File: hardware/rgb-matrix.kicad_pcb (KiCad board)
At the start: 4 copper layers, 58 x 58 mm, 84 parts, among them CON1 VEXT, P1 MATRIX_BOT, P10 PSOUTH, P11 PEAST, P12 WEST, P13 NORTH, P14 SOUTH, P15 EAST, P2 MATRIX_TOP, P3 SWD, P4 SPI3, P5 UART5, P6 VEXT, P7 USB_B, P8 PWEST, P9 PNORTH, SW1 RESET, SW2 BOOT, U1 74AC244, U2 74AC244, U3 74AC244, U4 ULN2803A, U5 STM32F405R, U6 LD3985M33R, U7 USBUFxxW6, X1 8MHz

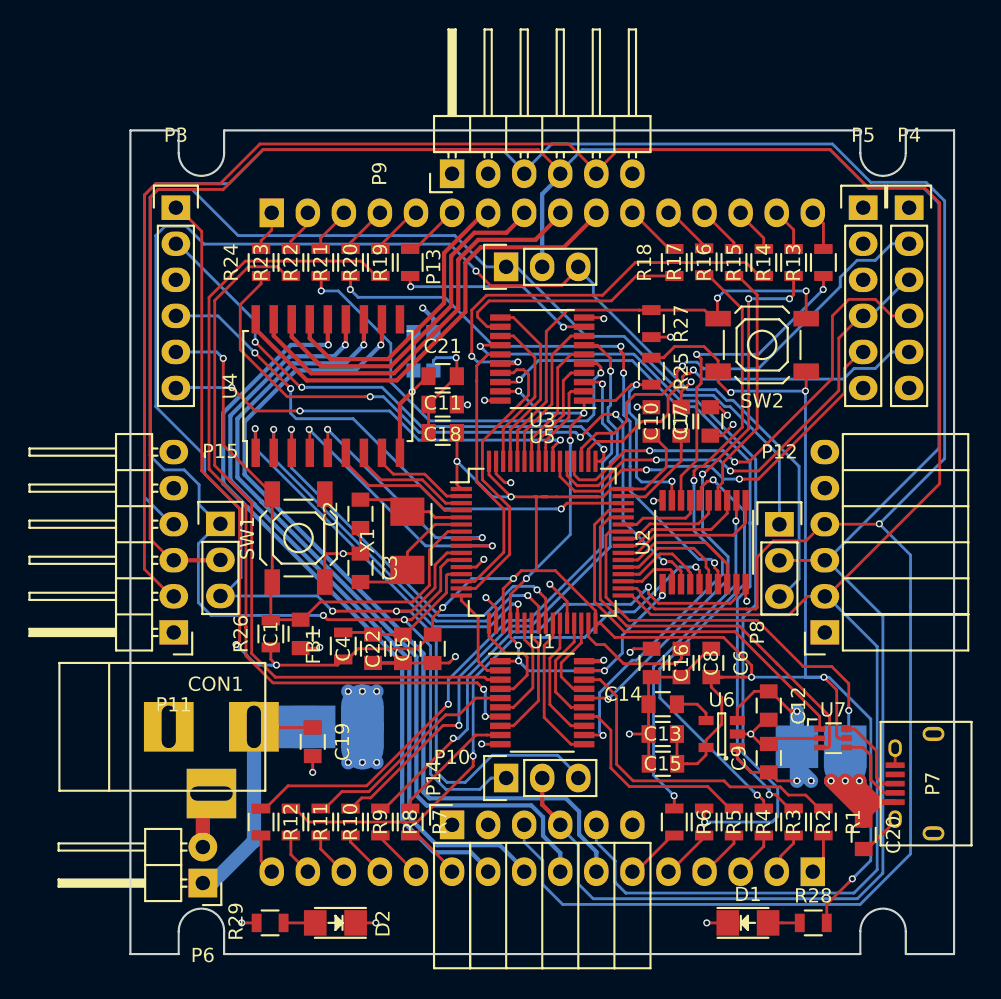
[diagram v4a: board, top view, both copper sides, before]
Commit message: Fix silkscreen
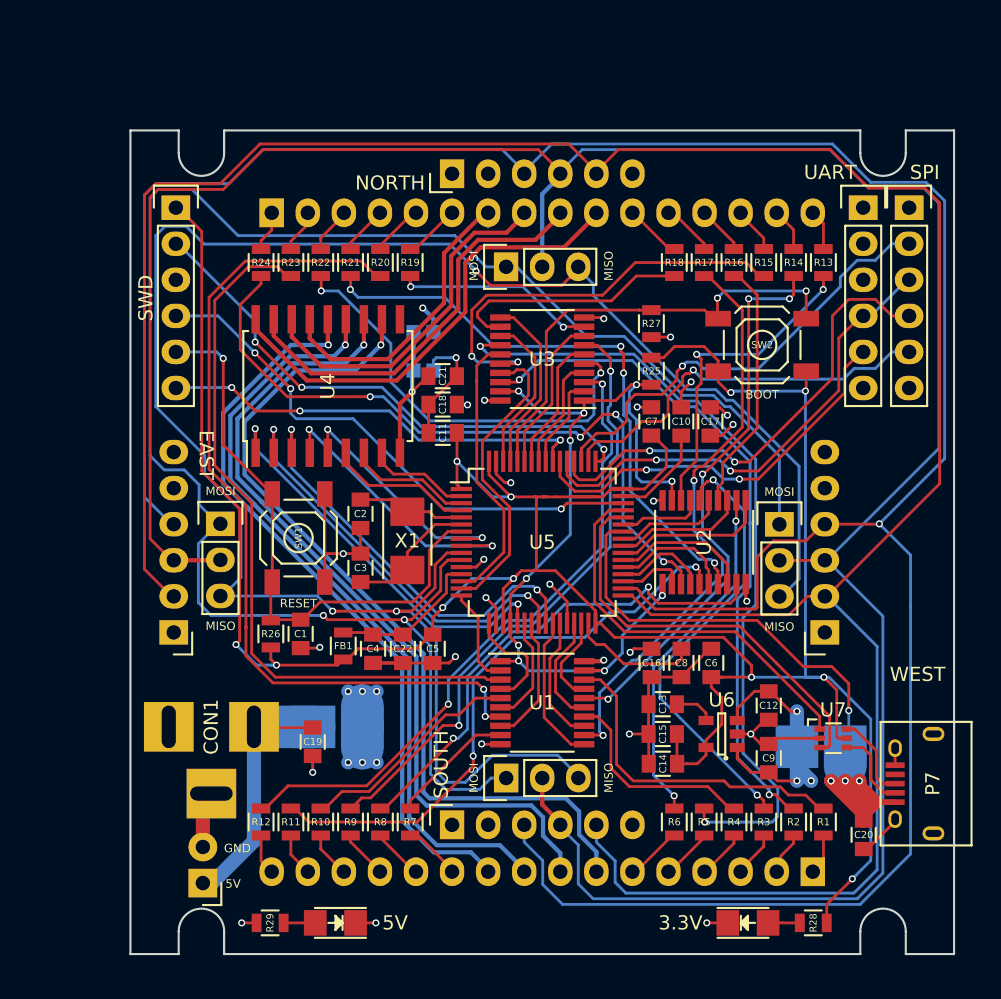
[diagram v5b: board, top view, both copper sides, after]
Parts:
- C1, C10, C11, C12, C13, C14, C15, C16, C17, C18, C19, C2, C20, C21, C22, C3, C4, C5, C6, C7, C8, C9: footprint Capacitors_SMD:C_0805 -> rgb-matrix:C_0805
- CON1: footprint Connect:BARREL_JACK -> rgb-matrix:BARREL_JACK
- FB1, R1, R10, R11, R12, R13, R14, R15, R16, R17, R18, R19, R2, R20, R21, R22, R23, R24, R25, R26, R27, R28, R29, R3, R4, R5, R6, R7, R8, R9: footprint Resistors_SMD:R_0805 -> rgb-matrix:R_0805
- P10, P8: footprint Socket_Strips:Socket_Strip_Angled_1x06 -> rgb-matrix:Socket_Strip_Angled_1x06
- P11, P9: footprint Pin_Headers:Pin_Header_Angled_1x06 -> rgb-matrix:Pin_Header_Angled_1x06
- P6: footprint Pin_Headers:Pin_Header_Angled_1x02 -> rgb-matrix:Pin_Header_Angled_1x02
- moved R17 0.05 mm to (173.6, 81.5)
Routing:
- net /power/VEXT: track 23.5 -> 21.4 mm
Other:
- board text added: "3.3V"
- board text added: "5V"
- board text added: "BOOT"
- board text added: "BOTTOM"
- board text added: "EAST"
- board text added: "GND"
- board text added: "MISO"
- board text added: "MOSI"
- board text added: "NORTH"
- board text added: "RESET"
- board text added: "SOUTH"
- board text added: "SPI"
- board text added: "SWD"
- board text added: "TOP"
- board text added: "UART"
- board text added: "WEST"

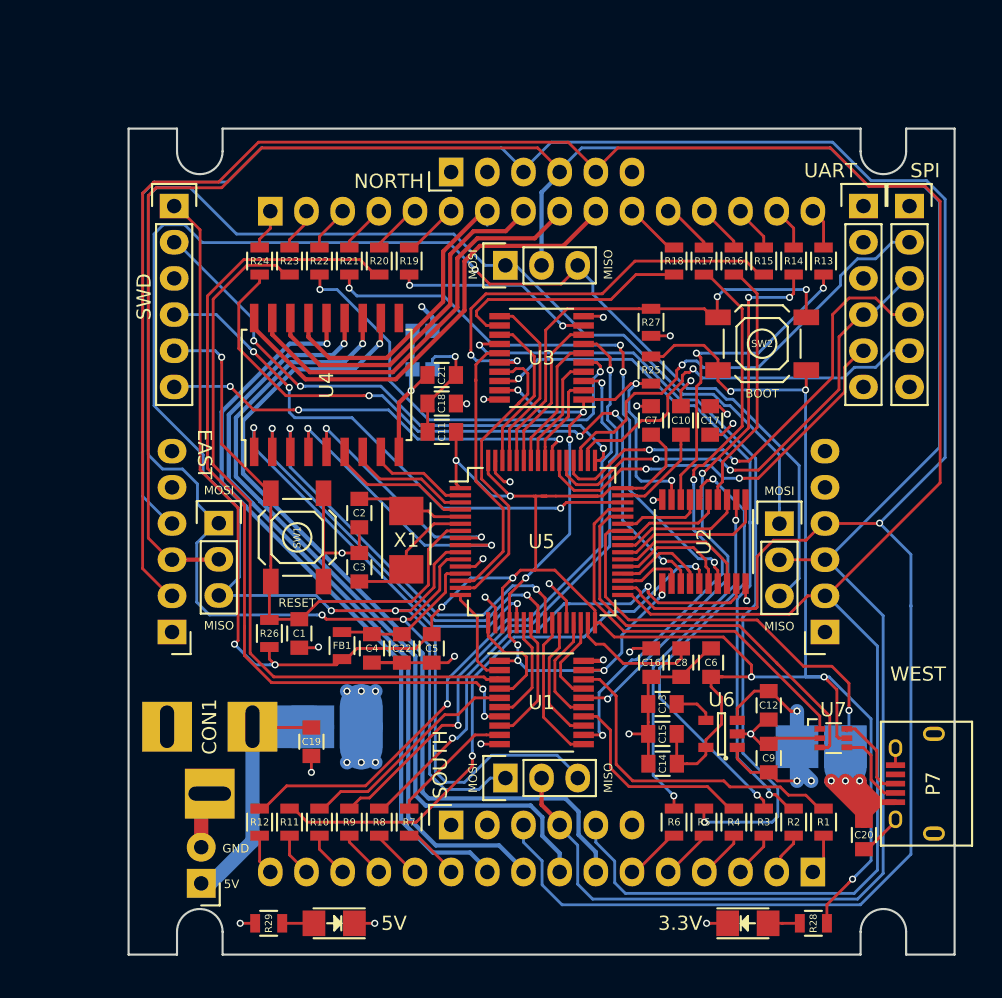
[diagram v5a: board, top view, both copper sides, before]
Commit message: Add 2nd GND pin for more curent + minor changes
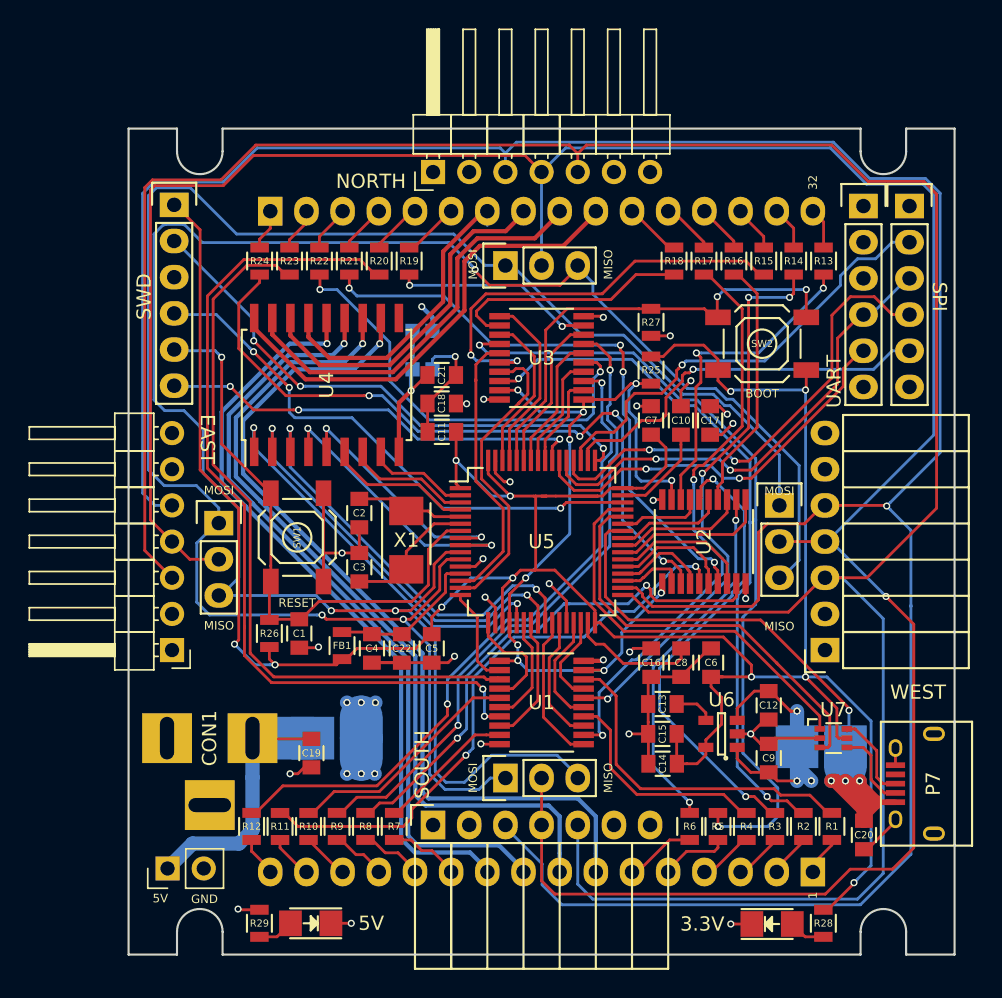
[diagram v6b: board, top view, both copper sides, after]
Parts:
- C16, C17, C18, C21: value 100n -> 100nF
- C2, C3: value 18pF -> 26pF
- P10, P8: footprint rgb-matrix:Socket_Strip_Angled_1x06 -> Socket_Strips:Socket_Strip_Angled_1x07
- P11, P9: footprint rgb-matrix:Pin_Header_Angled_1x06 -> Pin_Headers:Pin_Header_Angled_1x07_Pitch2.54mm
- P6: footprint rgb-matrix:Pin_Header_Angled_1x02 -> Pin_Headers:Pin_Header_Straight_1x02_Pitch2.54mm
- U7: value USBUFxxW6 -> USBUF01W6
- moved P6 2.59 mm to (135.9, 124.2), turned to 90 degrees
- moved D1 1.70 mm to (178.3, 128.1)
- moved D2 1.65 mm to (145.9, 128.0)
- moved P12 1.28 mm to (178.9, 98.7)
- moved P11 1.27 mm to (136.2, 108.8)
- moved P8 1.27 mm to (182.1, 108.8)
- moved P10 1.27 mm to (154.5, 121.1)
- moved P9 1.27 mm to (154.5, 75.2)
- moved R6 1.14 mm to (172.6, 121.2)
- moved R7 1.09 mm to (151.8, 121.2)
- moved R5 1.03 mm to (174.6, 121.2)
- moved R8 1.01 mm to (149.8, 121.2)
- moved R4 0.94 mm to (176.6, 121.2)
- moved R9 0.91 mm to (147.8, 121.2)
- moved R3 0.84 mm to (178.6, 121.2)
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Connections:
- P11 pad 2: SPI2_NSS -> GND
- P11 pad 3: /daisy/DATA -> SPI2_NSS
- P11 pad 4: SPI2_SCK -> /daisy/DATA
- P11 pad 5: +5V -> SPI2_SCK
- P8 pad 2: SPI2_NSS -> GND
- P8 pad 3: /daisy/DATA -> SPI2_NSS
- P8 pad 4: SPI2_SCK -> /daisy/DATA
- P8 pad 5: +5V -> SPI2_SCK
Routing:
- net SPI2_NSS: track 181.2 -> 185.8 mm
- net GND: track 82.3 -> 77.7 mm
- net +5V: track 44.5 -> 46.1 mm
- net +3V3: track 198.2 -> 196.7 mm
- net /matrix/5: track 3.65 -> 4.95 mm
- net /matrix/6: track 4.01 -> 5.23 mm
- net B8: track 46.0 -> 47.2 mm
- net G2: track 31.6 -> 32.7 mm
- net /matrix/11: track 4.09 -> 5.17 mm
- net R3: track 14.8 -> 15.8 mm
- net SPI2_SCK: track 190.0 -> 191.0 mm
- net B6: track 44.0 -> 45.0 mm
- net B1: track 48.2 -> 49.1 mm
- net /matrix/12: track 3.65 -> 4.61 mm
- net G5: track 36.0 -> 36.9 mm
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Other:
- board text added: "1"
- board text added: "32"

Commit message: Add more margin for the board to board connectors
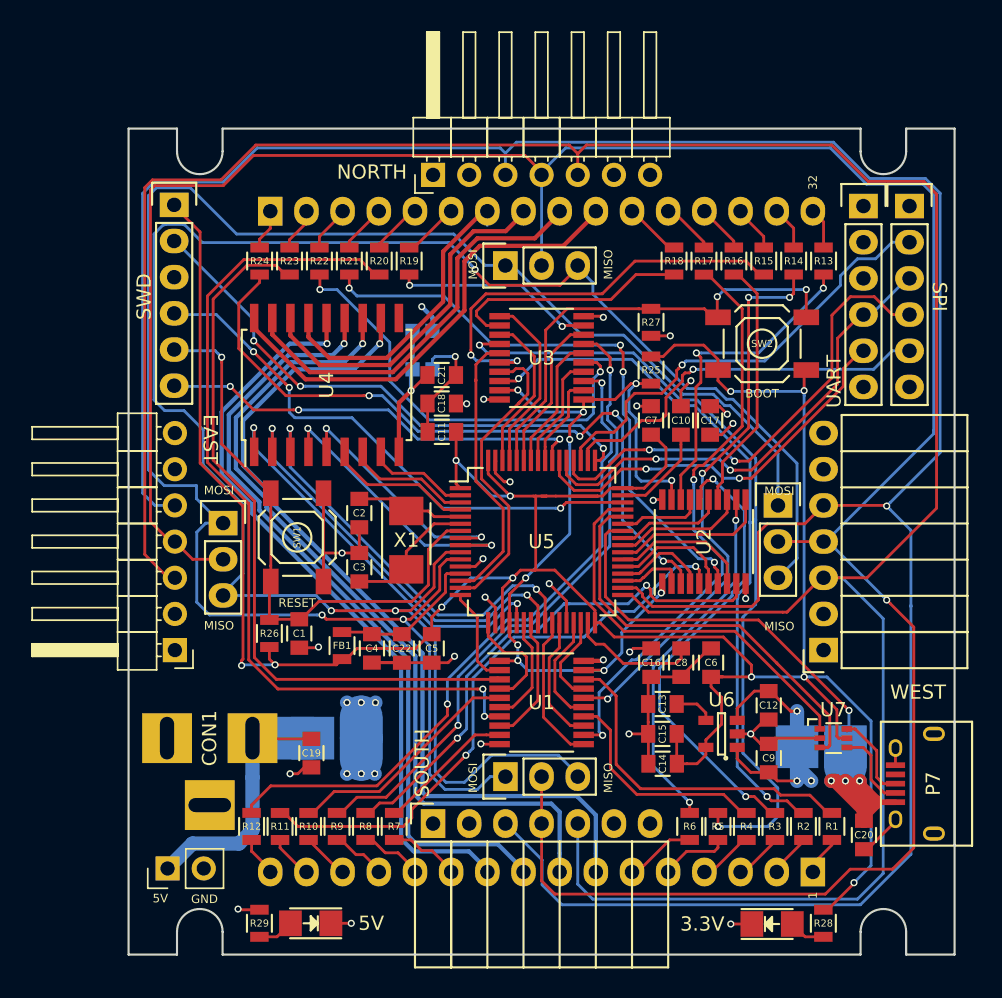
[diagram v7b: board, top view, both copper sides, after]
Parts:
- moved P15 0.30 mm to (139.8, 99.9)
- moved P9 0.20 mm to (154.5, 75.4)
- moved P11 0.20 mm to (136.4, 108.8)
- moved P10 0.10 mm to (154.5, 121.0)
- moved P12 0.10 mm to (178.8, 98.7)
- moved P14 0.10 mm to (159.6, 117.7)
- moved P8 0.10 mm to (182.0, 108.8)
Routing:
- net +5V: track 46.1 -> 44.7 mm
- net SPI2_MOSI: track 128.0 -> 128.9 mm
- net SPI2_NSS: track 185.8 -> 186.7 mm
- net SPI2_SCK: track 191.0 -> 191.8 mm
- net /daisy/DATA: track 184.5 -> 185.2 mm
- net B8: track 47.2 -> 47.8 mm
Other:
- rule via_min_drill: 0.254 -> 0.3

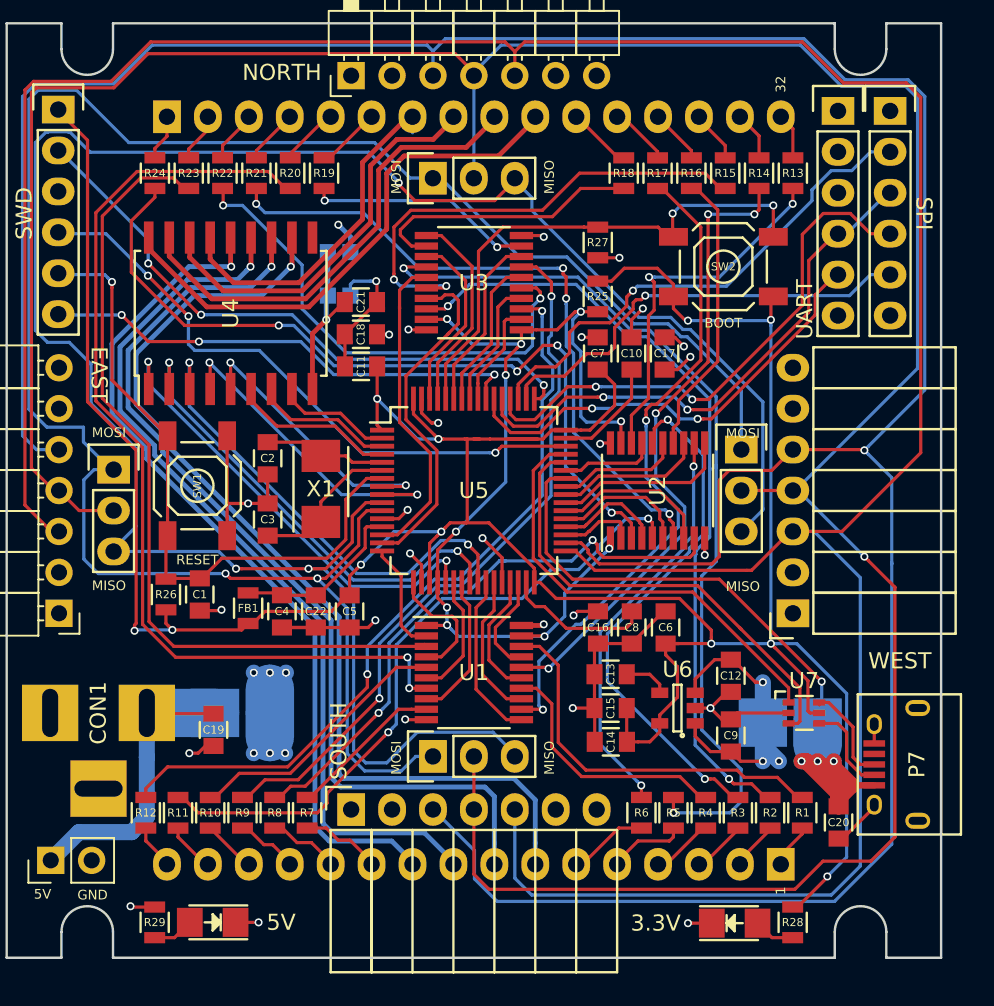
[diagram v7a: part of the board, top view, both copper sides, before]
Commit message: Cleanup tracks, fix 3d models
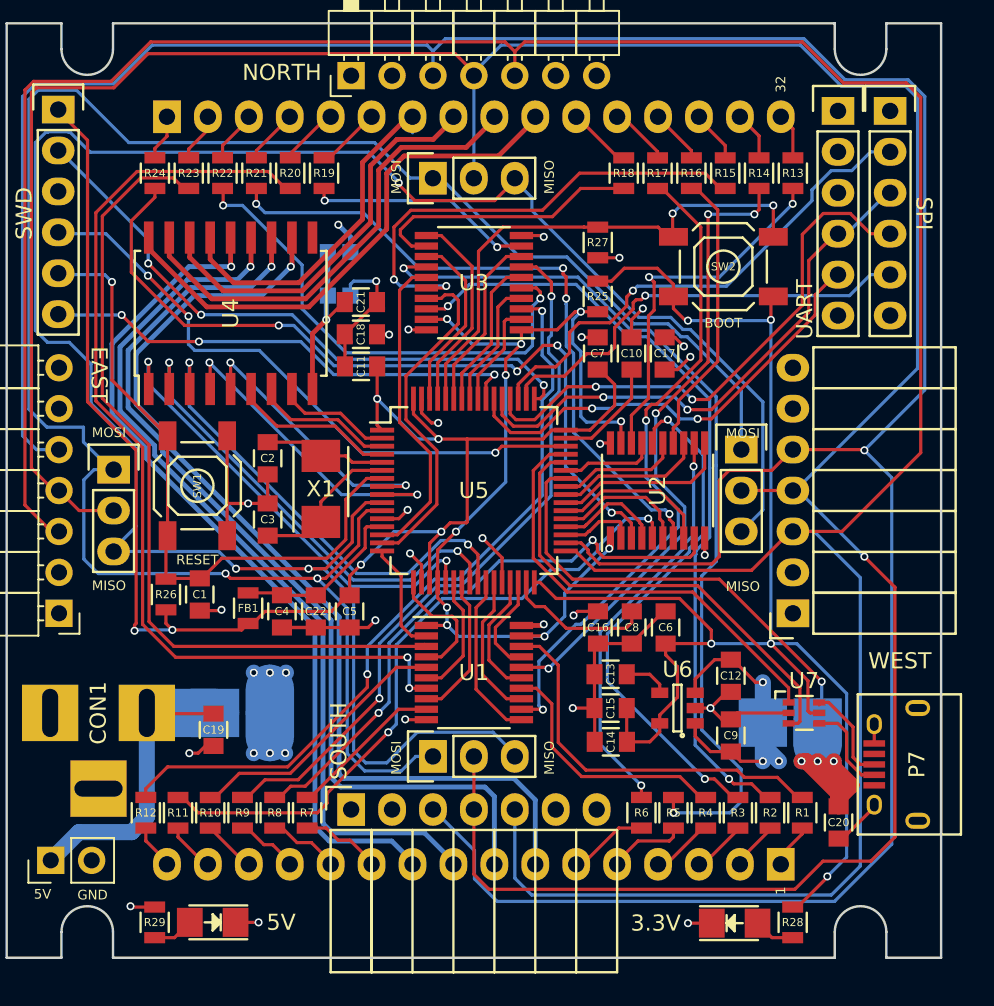
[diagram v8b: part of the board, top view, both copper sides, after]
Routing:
- net +3V3: track 197.2 -> 187.9 mm
- net VBUS: track 48.4 -> 45.7 mm
